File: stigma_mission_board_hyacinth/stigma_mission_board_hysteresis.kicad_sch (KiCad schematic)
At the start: 139 parts, among them J1 DF40C-70DS-0.4V(51), J10 JST-GH, J2 DF40C-70DS-0.4V(51), J6 SMA, J7 SMA, J8 RJ45_Wuerth_7499010211A, J9 JST-GH, Q1 AON7423, Q2 AO3400A, Q3 AO3401A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

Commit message: final adjustments for mission board rev2
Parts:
- D12: now not fitted
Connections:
- net bus_supply is gone; now on net charging_voltage: R3.1
- net at D2.1 (K), D3.1 (K), R1.1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: now also D12.1 (K)
- net at F1.2, J3.6 (Pin_6), J4.6 (Pin_6): no longer D12.1 (K)
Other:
- note added: "D12 allows powering the FC via the charging voltage. This can be useful in situations where we like to power the rocket does not use batteries."
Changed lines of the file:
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@@
 	(text "Vehicle Bus & Power Input"
 		(exclude_from_sim no)
-		(at 15.24 17.272 0)
+		(at 14.478 16.256 0)
 		(effects
 			(font
@@
 		)
 	)
+	(text "D12 allows powering the FC via the charging voltage. \nThis can be useful in situations where we like to power\nthe rocket does not use batteries."
+		(exclude_from_sim no)
+		(at 79.248 9.144 0)
+		(effects
+			(font
+				(size 1.27 1.27)
+			)
+		)
+	)
 	(text "S"
 		(exclude_from_sim no)
@@
 	)
 	(junction
-		(at 63.5 26.67)
-		(diameter 0)
-		(color 0 0 0 0)
-	)
-	(junction
 		(at 200.66 227.33)
 		(diameter 0)
@@
 	)
 	(junction
-		(at 55.88 24.13)
-		(diameter 0)
-		(color 0 0 0 0)
-	)
-	(junction
 		(at 391.16 204.47)
 		(diameter 0)
@@
 	)
 	(junction
+		(at 55.88 19.05)
+		(diameter 0)
+		(color 0 0 0 0)
+	)
+	(junction
 		(at 238.76 97.79)
 		(diameter 0)
@@
 	(wire
 		(pts
-			(xy 52.07 26.67) (xy 63.5 26.67)
-		)
-		(stroke
-			(width 0.4)
-			(type default)
-			(color 255 10 0 1)
-		)
-	)
-	(wire
-		(pts
 			(xy 210.82 146.05) (xy 212.09 146.05)
 		)
@@
 	(wire
 		(pts
-			(xy 63.5 24.13) (xy 63.5 26.67)
-		)
-		(stroke
-			(width 0)
-			(type default)
-		)
-	)
-	(wire
-		(pts
 			(xy 287.02 227.33) (xy 292.1 227.33)
 		)
@@
 	(wire
 		(pts
-			(xy 63.5 26.67) (xy 67.31 26.67)
+			(xy 52.07 26.67) (xy 67.31 26.67)
 		)
 		(stroke
@@
 	(wire
 		(pts
+			(xy 67.31 19.05) (xy 111.76 19.05)
+		)
+		(stroke
+			(width 0)
+			(type default)
+		)
+	)
+	(wire
+		(pts
 			(xy 130.81 208.28) (xy 149.86 208.28)
 		)
@@
 	(wire
 		(pts
+			(xy 55.88 19.05) (xy 55.88 24.13)
+		)
+		(stroke
+			(width 0)
+			(type default)
+		)
+	)
+	(wire
+		(pts
 			(xy 251.46 97.79) (xy 251.46 100.33)
 		)
@@
 	(wire
 		(pts
+			(xy 130.81 27.94) (xy 111.76 27.94)
+		)
+		(stroke
+			(width 0)
+			(type default)
+		)
+	)
+	(wire
+		(pts
 			(xy 154.94 27.94) (xy 162.56 27.94)
 		)
@@
 	(wire
 		(pts
+			(xy 111.76 19.05) (xy 111.76 27.94)
+		)
+		(stroke
+			(width 0)
+			(type default)
+		)
+	)
+	(wire
+		(pts
 			(xy 49.53 26.67) (xy 52.07 26.67)
 		)
@@
 	(wire
 		(pts
+			(xy 59.69 19.05) (xy 55.88 19.05)
+		)
+		(stroke
+			(width 0)
+			(type default)
+		)
+	)
+	(wire
+		(pts
 			(xy 199.39 229.87) (xy 203.2 229.87)
 		)
@@
 	(symbol
 		(lib_id "Diode:SS34")
-		(at 59.69 24.13 180)
+		(at 63.5 19.05 180)
 		(unit 1)
 		(exclude_from_sim no)
 		(in_bom yes)
 		(on_board yes)
-		(dnp no)
+		(dnp yes)
 		(property "Reference" "D12"
-			(at 62.992 22.86 0)
+			(at 65.532 16.51 0)
 			(effects
 				(font
@@
 		)
 		(property "Value" "SS34"
-			(at 67.31 22.86 0)
+			(at 60.706 16.51 0)
 			(effects
 				(font
@@
 		)
 		(property "Footprint" "Diode_SMD:D_SMA"
-			(at 59.69 19.685 0)
+			(at 63.5 14.605 0)
 			(effects
 				(font
@@
 		)
 		(property "Datasheet" "https://www.vishay.com/docs/88751/ss32.pdf"
-			(at 59.69 24.13 0)
+			(at 63.5 19.05 0)
 			(effects
 				(font
@@
 		)
 		(property "Description" ""
-			(at 59.69 24.13 0)
+			(at 63.5 19.05 0)
 			(effects
 				(font
@@
 		)
 		(property "LCSC #" ""
-			(at 59.69 24.13 0)
+			(at 63.5 19.05 0)
 			(effects
 				(font
@@
 		)
 		(property "DigiKey#" ""
-			(at 59.69 24.13 0)
+			(at 63.5 19.05 0)
 			(effects
 				(font
@@
 		)
 		(property "LCSC" "C8678"
-			(at 59.69 19.558 0)
+			(at 63.246 14.478 0)
 			(effects
 				(font
@@
 		)
 		(property "Value" "33"
-			(at 147.066 251.714 90)
+			(at 145.542 251.714 90)
 			(effects
 				(font
@@
 		)
 		(property "LCSC" "C25161"
-			(at 142.24 252.73 0)
+			(at 142.494 253.746 90)
 			(effects
 				(font
@@
 		)
 		(property "Value" "bus_main"
-			(at 78.994 19.304 0)
+			(at 78.74 20.32 0)
 			(effects
 				(font
@@
 	(symbol
 		(lib_id "power:+VSW")
-		(at 55.88 22.86 0)
+		(at 55.88 19.05 0)
 		(unit 1)
 		(exclude_from_sim no)
@@
 		(dnp no)
 		(property "Reference" "#PWR01"
-			(at 55.88 26.67 0)
+			(at 55.88 22.86 0)
 			(effects
 				(font
@@
 		)
 		(property "Value" "charging_voltage"
-			(at 56.896 16.764 0)
+			(at 56.642 23.114 0)
 			(effects
 				(font
@@
 		)
 		(property "Footprint" ""
-			(at 55.88 22.86 0)
+			(at 55.88 19.05 0)
 			(effects
 				(font
@@
 		)
 		(property "Datasheet" ""
-			(at 55.88 22.86 0)
+			(at 55.88 19.05 0)
 			(effects
 				(font
@@
 		)
 		(property "Description" ""
-			(at 55.88 22.86 0)
+			(at 55.88 19.05 0)
 			(effects
 				(font
@@
 			)
 		)
-		(property "Value" "bus_supply"
+		(property "Value" "charging_voltage"
 			(at 251.46 20.32 0)
 			(effects
@@
 		)
 		(property "LCSC" "C25744"
-			(at 149.86 217.17 0)
+			(at 149.606 217.17 0)
 			(effects
 				(font
@@
 		)
 		(property "Value" "recovery"
-			(at 95.504 19.304 0)
+			(at 94.742 20.574 0)
 			(effects
 				(font

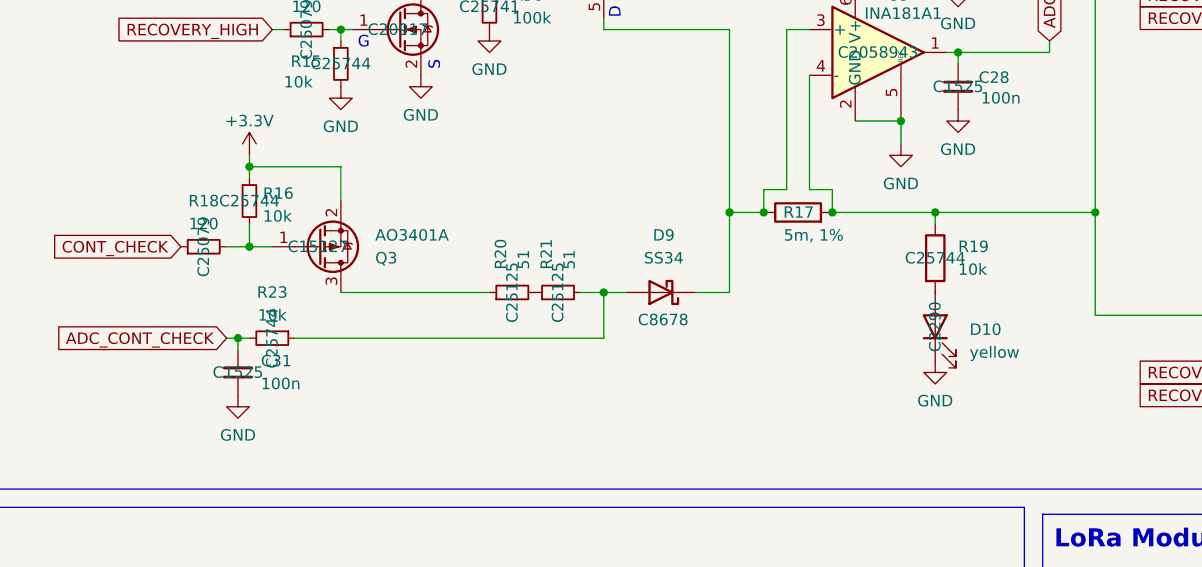
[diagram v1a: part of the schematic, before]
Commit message: improve can traces at VB, use smaller resistor for voltage reg.
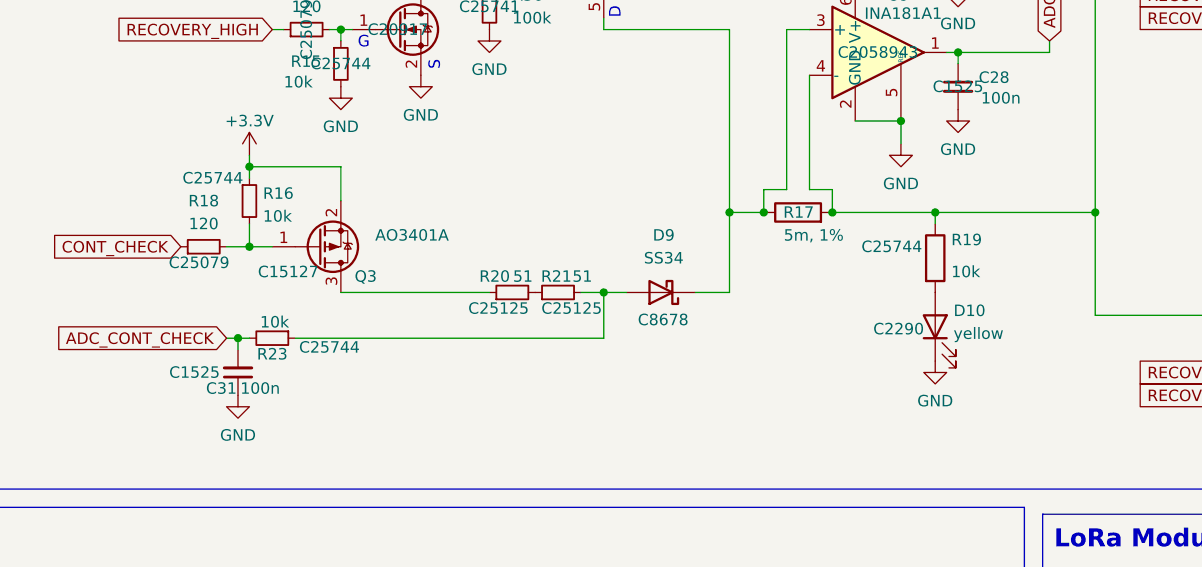
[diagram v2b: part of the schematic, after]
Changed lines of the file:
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@@
 		(on_board yes)
 		(dnp no)
-		(fields_autoplaced yes)
 		(property "Reference" "R21"
-			(at 245.1099 138.43 0)
+			(at 247.904 139.192 90)
 			(effects
 				(font
@@
 		)
 		(property "Value" "51"
-			(at 247.6499 138.43 0)
+			(at 250.19 139.192 90)
 			(effects
 				(font
@@
 		)
 		(property "LCSC" "C25125"
-			(at 246.38 140.97 0)
+			(at 247.904 142.748 90)
 			(effects
 				(font
@@
 		(on_board yes)
 		(dnp no)
-		(fields_autoplaced yes)
 		(property "Reference" "R16"
 			(at 213.5886 129.9753 0)
@@
 		)
 		(property "LCSC" "C25744"
-			(at 212.09 130.81 0)
+			(at 208.026 128.27 0)
 			(effects
 				(font
@@
 		(on_board yes)
 		(dnp no)
-		(fields_autoplaced yes)
 		(property "Reference" "R19"
-			(at 290.83 135.8899 0)
+			(at 290.068 135.128 0)
 			(effects
 				(font
@@
 		)
 		(property "Value" "10k"
-			(at 290.83 138.4299 0)
+			(at 290.068 138.684 0)
 			(effects
 				(font
@@
 		)
 		(property "LCSC" "C25744"
-			(at 288.29 137.16 0)
+			(at 283.464 135.89 0)
 			(effects
 				(font
@@
 		(dnp no)
 		(property "Reference" "Q3"
-			(at 226.06 137.1601 0)
+			(at 223.774 139.192 0)
 			(effects
 				(font
@@
 		)
 		(property "LCSC" "C15127"
-			(at 219.71 135.89 0)
+			(at 216.408 138.684 0)
 			(effects
 				(font
@@
 		(on_board yes)
 		(dnp no)
-		(fields_autoplaced yes)
 		(property "Reference" "R23"
-			(at 214.63 140.97 90)
+			(at 214.63 147.828 90)
 			(effects
 				(font
@@
 		)
 		(property "Value" "10k"
-			(at 214.63 143.51 90)
+			(at 214.884 144.272 90)
 			(effects
 				(font
@@
 		)
 		(property "LCSC" "C25744"
-			(at 214.63 146.05 0)
+			(at 220.98 147.066 90)
 			(effects
 				(font
@@
 		(on_board yes)
 		(dnp no)
-		(fields_autoplaced yes)
 		(property "Reference" "R20"
-			(at 240.0299 138.43 0)
+			(at 241.046 139.192 90)
 			(effects
 				(font
@@
 		)
 		(property "Value" "51"
-			(at 242.5699 138.43 0)
+			(at 243.586 139.192 90)
 			(effects
 				(font
@@
 		)
 		(property "LCSC" "C25125"
-			(at 241.3 140.97 0)
+			(at 239.776 142.748 90)
 			(effects
 				(font
@@
 		(on_board yes)
 		(dnp no)
-		(fields_autoplaced yes)
 		(property "Reference" "R18"
 			(at 207.01 130.81 90)
@@
 		)
 		(property "LCSC" "C25079"
-			(at 207.01 135.89 0)
+			(at 206.502 137.668 90)
 			(effects
 				(font
@@
 		(on_board yes)
 		(dnp no)
-		(fields_autoplaced yes)
 		(property "Reference" "D10"
-			(at 292.1 145.0974 90)
+			(at 290.322 143.002 90)
 			(effects
 				(font
@@
 		)
 		(property "Value" "yellow"
-			(at 292.1 147.6374 90)
+			(at 290.322 145.542 90)
 			(effects
 				(font
@@
 		)
 		(property "LCSC" "C2290"
-			(at 288.29 144.78 0)
+			(at 284.226 145.034 90)
 			(effects
 				(font
@@
 		(on_board yes)
 		(dnp no)
-		(fields_autoplaced yes)
 		(property "Reference" "C31"
-			(at 213.36 148.5835 0)
+			(at 207.264 151.638 0)
 			(effects
 				(font
@@
 		)
 		(property "Value" "100n"
-			(at 213.36 151.1235 0)
+			(at 211.074 151.638 0)
 			(effects
 				(font
@@
 		)
 		(property "LCSC" "C1525"
-			(at 210.82 149.86 0)
+			(at 205.994 149.86 0)
 			(effects
 				(font

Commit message: remove cont check and rec jumper
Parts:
- removed C31: 100n, Capacitor_SMD:C_0402_1005Metric, symbol Device:C_Small
- removed D9: SS34, Diode_SMD:D_SMA, symbol Diode:SS34
- removed Q3: AO3401A, Package_TO_SOT_SMD:SOT-23, symbol Transistor_FET:AO3401A
- removed R16, R23: 10k, Resistor_SMD:R_0402_1005Metric, symbol Device:R_Small
- removed R18: 120, Resistor_SMD:R_0402_1005Metric, symbol Device:R_Small
- removed R20, R21: 51, Resistor_SMD:R_0402_1005Metric, symbol Device:R_Small
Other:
- moved on the sheet: Q1, Q2, R12, R14, R15, R56

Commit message: design check finished, some cosmetic changes, part adaptions, prints, etc.
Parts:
- added TP1, TP2, TP3, TP4, TP5, TP6, TP7: TestPoint, TestPoint:TestPoint_Pad_D1.5mm, symbol Connector:TestPoint
- D10: value yellow -> white
- F1: value 1.5A -> 3A; footprint Fuse:Fuse_1206_3216Metric -> Fuse:Fuse_1206_3216Metric_Pad1.42x1.75mm_HandSolder; DigiKey# 507-1805-1-ND -> (none); LCSC (none) -> C99558; Manufacturer Bel Fuse Inc. -> Littelfuse; Part# 0ZCJ0075AF2E -> 0467003.NRHF
- U4: value INA181A1 -> INA181A3; LCSC C2058943 -> C2652255
- U9: value INA181A1 -> INA181A2; LCSC C2058943 -> C2058784
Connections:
- net +3.3V: now also TP7.1
- net +5V: now also TP3.1
- net UART4_RX: now also TP1.1
- net UART4_TX: now also TP2.1
- net vdd_ethernet: now also TP4.1
- net vdd_lora1: now also TP6.1
- net vdd_lora2: now also TP5.1
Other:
- note added: "@todo: correct fuse?!"
- note added: "changed to A2 -> higher gain"
- note added: "changed to A3 -> higher gain"
- note added: "flyback?"
- moved on the sheet: R51, R52

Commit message: finished req. checklist, marginal changes
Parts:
- J3, J4, J5, J6, J7, J8: now not fitted
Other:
- note removed: "@todo: correct fuse?!"
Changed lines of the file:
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@@
 		)
 	)
-	(text "@todo: \ncorrect fuse?!"
-		(exclude_from_sim no)
-		(at 69.088 36.322 0)
-		(effects
-			(font
-				(size 1.27 1.27)
-			)
-		)
-	)
 	(text "D12 allows powering the FC via the charging voltage. \nThis can be useful in situations where we like to power\nthe rocket does not use batteries."
 		(exclude_from_sim no)
@@
 		(in_bom yes)
 		(on_board yes)
-		(dnp no)
+		(dnp yes)
 		(fields_autoplaced yes)
 		(property "Reference" "J7"
@@
 		(in_bom yes)
 		(on_board yes)
-		(dnp no)
+		(dnp yes)
 		(fields_autoplaced yes)
 		(property "Reference" "J8"
@@
 		(in_bom yes)
 		(on_board yes)
-		(dnp no)
+		(dnp yes)
 		(fields_autoplaced yes)
 		(property "Reference" "J6"
@@
 		(in_bom yes)
 		(on_board yes)
-		(dnp no)
+		(dnp yes)
 		(property "Reference" "J5"
 			(at 373.38 121.412 0)
@@
 		(in_bom yes)
 		(on_board yes)
-		(dnp no)
+		(dnp yes)
 		(property "Reference" "J3"
 			(at 40.64 21.336 0)
@@
 		(in_bom yes)
 		(on_board yes)
-		(dnp no)
+		(dnp yes)
 		(property "Reference" "J4"
 			(at 40.64 36.576 0)

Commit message: some lcsc number changes
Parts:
- F1: LCSC C99558 -> C2838898
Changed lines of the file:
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@@
 			)
 		)
-		(property "LCSC" "C99558"
+		(property "LCSC" "C2838898"
 			(at 69.85 26.67 90)
 			(effects

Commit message: added schematic as pdf
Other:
- title: Stigma mission board -> Zephyr mission board
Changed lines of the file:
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@@
 	(paper "A3")
 	(title_block
-		(title "Stigma mission board")
-		(date "2024-12-16")
+		(title "Zephyr mission board")
+		(date "2026-05-04")
 		(rev "v2")
 		(company "TUDSaT")
